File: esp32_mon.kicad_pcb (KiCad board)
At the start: 2 copper layers, 38.7 x 49.5 mm, 31 parts, among them J1 I2C, J2 UART, J3 BAT, J4 USB, Q1 NTJD1155L, Q2 MMDT3904, U1 ESP32, U2 TC4054GR, U3 RT9080-33GJ5S, U4 SHT40

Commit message: cleanup old project
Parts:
- U4: value SHT40 -> SHT4x; footprint SHT40:SHT40-AD1B-R2 -> parts:SHT4x
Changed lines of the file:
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@@
     (fp_line (start 0.88 1.45) (end -0.88 1.45) (layer "F.Fab") (width 0.1))
     (pad "1" smd rect locked (at -1.71 -0.95 90) (size 2 0.65) (layers "F.Cu" "F.Paste" "F.Mask")
-      (net 22 "Net-(R1-Pad2)") (pinfunction "CHRG") (pintype "unspecified"))
+      (net 22 "Net-(R1-Pad2)") (pinfunction "CHRG") (pintype "output"))
     (pad "2" smd rect locked (at -1.71 0 90) (size 2 0.65) (layers "F.Cu" "F.Paste" "F.Mask")
       (net 1 "GND") (pinfunction "GND") (pintype "power_in"))
     (pad "3" smd rect locked (at -1.71 0.95 90) (size 2 0.65) (layers "F.Cu" "F.Paste" "F.Mask")
-      (net 4 "+BATT") (pinfunction "BAT") (pintype "unspecified"))
+      (net 4 "+BATT") (pinfunction "BAT") (pintype "power_out"))
     (pad "4" smd rect locked (at 1.71 0.95 90) (size 2 0.65) (layers "F.Cu" "F.Paste" "F.Mask")
       (net 3 "VCC") (pinfunction "VCC") (pintype "power_in"))
     (pad "5" smd rect locked (at 1.71 -0.95 90) (size 2 0.65) (layers "F.Cu" "F.Paste" "F.Mask")
-      (net 23 "Net-(R2-Pad1)") (pinfunction "PROG") (pintype "unspecified"))
+      (net 23 "Net-(R2-Pad1)") (pinfunction "PROG") (pintype "input"))
     (model "${KICAD6_3DMODEL_DIR}/Package_TO_SOT_SMD.3dshapes/TSOT-23-5.wrl"
       (offset (xyz 0 0 0))
@@
       (net 24 "unconnected-(U3-Pad4)") (pinfunction "NC") (pintype "no_connect"))
     (pad "5" smd rect locked (at 1.71 -0.95 90) (size 2 0.65) (layers "F.Cu" "F.Paste" "F.Mask")
-      (net 2 "+3V3") (pinfunction "VOUT") (pintype "output"))
+      (net 2 "+3V3") (pinfunction "VOUT") (pintype "power_out"))
     (model "${KISYS3DMOD}/Package_TO_SOT_SMD.3dshapes/TSOT-23-5.wrl"
       (offset (xyz 0 0 0))
@@
     )
   )
-  (footprint "SHT40:SHT40-AD1B-R2" (layer "F.Cu")
+  (footprint "parts:SHT4x" (layer "F.Cu")
     (at 183.007 57.658 180)
     (property "Sheetfile" "esp32_mon.kicad_sch")
     (property "Sheetname" "")
     (attr through_hole)
-    (fp_text reference "U4" (at 0 2.54) (layer "F.SilkS") hide
-      (effects (font (size 1 1) (thickness 0.15)))
-    )
-    (fp_text value "SHT40" (at 2.54 0 270) (layer "F.SilkS")
-      (effects (font (size 1 1) (thickness 0.15)))
-    )
-    (fp_text user "*" (at 0 0) (layer "F.SilkS")
-      (effects (font (size 1 1) (thickness 0.15)))
-    )
-    (fp_text user "Copyright 2021 Accelerated Designs. All rights reserved." (at 0 0) (layer "Cmts.User")
+    (fp_text reference "U4" (at 0 2.54 180) (layer "F.SilkS")
+      (effects (font (size 1 1) (thickness 0.15)))
+    )
+    (fp_text value "SHT4x" (at 0 -2.54 180) (layer "F.SilkS")
+      (effects (font (size 1 1) (thickness 0.15)))
+    )
+    (fp_text user "*" (at 0 0 180) (layer "F.SilkS")
+      (effects (font (size 1 1) (thickness 0.15)))
+    )
+    (fp_text user "Copyright 2021 Accelerated Designs. All rights reserved." (at 0 0 180) (layer "Cmts.User")
       (effects (font (size 0.127 0.127) (thickness 0.002)))
     )
-    (fp_text user "*" (at 0 0) (layer "F.Fab")
-      (effects (font (size 1 1) (thickness 0.15)))
-    )
+    (fp_text user "*" (at 0 0 180) (layer "F.Fab")
+      (effects (font (size 1 1) (thickness 0.15)))
+    )
+    (fp_line (start -0.9271 0.9271) (end 0.9271 0.9271) (layer "F.SilkS") (width 0.12))
     (fp_line (start 0.9271 -0.9271) (end -0.9271 -0.9271) (layer "F.SilkS") (width 0.12))
-    (fp_line (start -0.9271 0.9271) (end 0.9271 0.9271) (layer "F.SilkS") (width 0.12))
     (fp_circle (center -1.950899 -0.4) (end -1.849299 -0.4) (layer "F.SilkS") (width 0.12) (fill none))
-    (fp_line (start -1.0541 1.0541) (end -1.0541 0.8068) (layer "F.CrtYd") (width 0.05))
-    (fp_line (start 1.0541 0.8068) (end 1.0541 1.0541) (layer "F.CrtYd") (width 0.05))
-    (fp_line (start 1.0541 -1.0541) (end 1.0541 -0.8068) (layer "F.CrtYd") (width 0.05))
+    (fp_line (start -1.0541 -0.8068) (end -1.0541 -1.0541) (layer "F.CrtYd") (width 0.05))
     (fp_line (start -1.0541 -1.0541) (end 1.0541 -1.0541) (layer "F.CrtYd") (width 0.05))
-    (fp_line (start 1.354099 -0.8068) (end 1.354099 0.8068) (layer "F.CrtYd") (width 0.05))
-    (fp_line (start -1.0541 -0.8068) (end -1.0541 -1.0541) (layer "F.CrtYd") (width 0.05))
-    (fp_line (start 1.354099 0.8068) (end 1.0541 0.8068) (layer "F.CrtYd") (width 0.05))
-    (fp_line (start -1.354099 -0.8068) (end -1.0541 -0.8068) (layer "F.CrtYd") (width 0.05))
-    (fp_line (start -1.0541 0.8068) (end -1.354099 0.8068) (layer "F.CrtYd") (width 0.05))
     (fp_line (start -1.354099 0.8068) (end -1.354099 -0.8068) (layer "F.CrtYd") (width 0.05))
     (fp_line (start 1.0541 1.0541) (end -1.0541 1.0541) (layer "F.CrtYd") (width 0.05))
+    (fp_line (start -1.354099 -0.8068) (end -1.0541 -0.8068) (layer "F.CrtYd") (width 0.05))
+    (fp_line (start 1.354099 -0.8068) (end 1.354099 0.8068) (layer "F.CrtYd") (width 0.05))
     (fp_line (start 1.0541 -0.8068) (end 1.354099 -0.8068) (layer "F.CrtYd") (width 0.05))
+    (fp_line (start 1.0541 -1.0541) (end 1.0541 -0.8068) (layer "F.CrtYd") (width 0.05))
+    (fp_line (start 1.354099 0.8068) (end 1.0541 0.8068) (layer "F.CrtYd") (width 0.05))
+    (fp_line (start -1.0541 1.0541) (end -1.0541 0.8068) (layer "F.CrtYd") (width 0.05))
+    (fp_line (start -1.0541 0.8068) (end -1.354099 0.8068) (layer "F.CrtYd") (width 0.05))
+    (fp_line (start 1.0541 0.8068) (end 1.0541 1.0541) (layer "F.CrtYd") (width 0.05))
     (fp_circle (center -1.601699 -0.4) (end -1.525499 -0.4) (layer "F.CrtYd") (width 0.05) (fill none))
+    (fp_line (start -0.8001 -0.8001) (end -0.8001 0.8001) (layer "F.Fab") (width 0.1))
     (fp_line (start -0.8001 0.8001) (end 0.8001 0.8001) (layer "F.Fab") (width 0.1))
-    (fp_line (start -0.8001 -0.8001) (end -0.8001 0.8001) (layer "F.Fab") (width 0.1))
     (fp_line (start 0.8001 -0.8001) (end -0.8001 -0.8001) (layer "F.Fab") (width 0.1))
     (fp_line (start 0.8001 0.8001) (end 0.8001 -0.8001) (layer "F.Fab") (width 0.1))

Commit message: minor cleanup
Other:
- board text added: "ESPmon 2.0"
- board text removed: "ESPmon rev2.0"
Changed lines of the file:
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@@
       (effects (font (size 1 1) (thickness 0.15)))
     )
-    (fp_text value "SHT4x" (at 0 -2.54 180) (layer "F.SilkS")
+    (fp_text value "SHT4x" (at 2.667 0 270) (layer "F.SilkS")
       (effects (font (size 1 1) (thickness 0.15)))
     )
@@
     (effects (font (size 1 1) (thickness 0.15)) (justify mirror))
   )
-  (gr_text "ESPmon\nrev2.0" (at 154.94 48.514) (layer "F.SilkS")
+  (gr_text "ESPmon\n2.0" (at 154.94 48.514) (layer "F.SilkS")
     (effects (font (size 1.5 1.5) (thickness 0.3)))
   )
@@
   (via (at 164.465 54.61) (size 0.8) (drill 0.4) (layers "F.Cu" "B.Cu") (free) (net 1))
   (via (at 172.72 64.77) (size 0.8) (drill 0.4) (layers "F.Cu" "B.Cu") (free) (net 1))
-  (via (at 163.195 90.17) (size 0.8) (drill 0.4) (layers "F.Cu" "B.Cu") (free) (net 1))
+  (via (at 151.511 68.453) (size 0.8) (drill 0.4) (layers "F.Cu" "B.Cu") (free) (net 1))
   (via (at 186.69 52.959) (size 0.8) (drill 0.4) (layers "F.Cu" "B.Cu") (free) (net 1))
   (via (at 186.69 88.265) (size 0.8) (drill 0.4) (layers "F.Cu" "B.Cu") (free) (net 1))
@@
   (via (at 180.975 58.42) (size 0.8) (drill 0.4) (layers "F.Cu" "B.Cu") (free) (net 1))
   (via (at 172.72 54.61) (size 0.8) (drill 0.4) (layers "F.Cu" "B.Cu") (free) (net 1))
-  (via (at 153.67 90.805) (size 0.8) (drill 0.4) (layers "F.Cu" "B.Cu") (free) (net 1))
+  (via (at 153.797 90.297) (size 0.8) (drill 0.4) (layers "F.Cu" "B.Cu") (free) (net 1))
   (segment (start 156.9935 54.1235) (end 156.845 53.975) (width 0.5) (layer "F.Cu") (net 2))
   (segment (start 175.641 72.898) (end 178.943 72.898) (width 0.25) (layer "F.Cu") (net 2))
@@
   (segment (start 152.908 83.312) (end 154.178 82.042) (width 0.25) (layer "F.Cu") (net 8))
   (segment (start 153.42501 75.82499) (end 154.94 74.31) (width 0.25) (layer "F.Cu") (net 8))
-  (segment (start 152.4 78.74) (end 152.4 78.724) (width 0.25) (layer "F.Cu") (net 8))
   (segment (start 153.42501 77.69899) (end 153.42501 75.82499) (width 0.25) (layer "F.Cu") (net 8))
   (segment (start 154.94 80.01) (end 154.686 79.756) (width 0.25) (layer "F.Cu") (net 8))

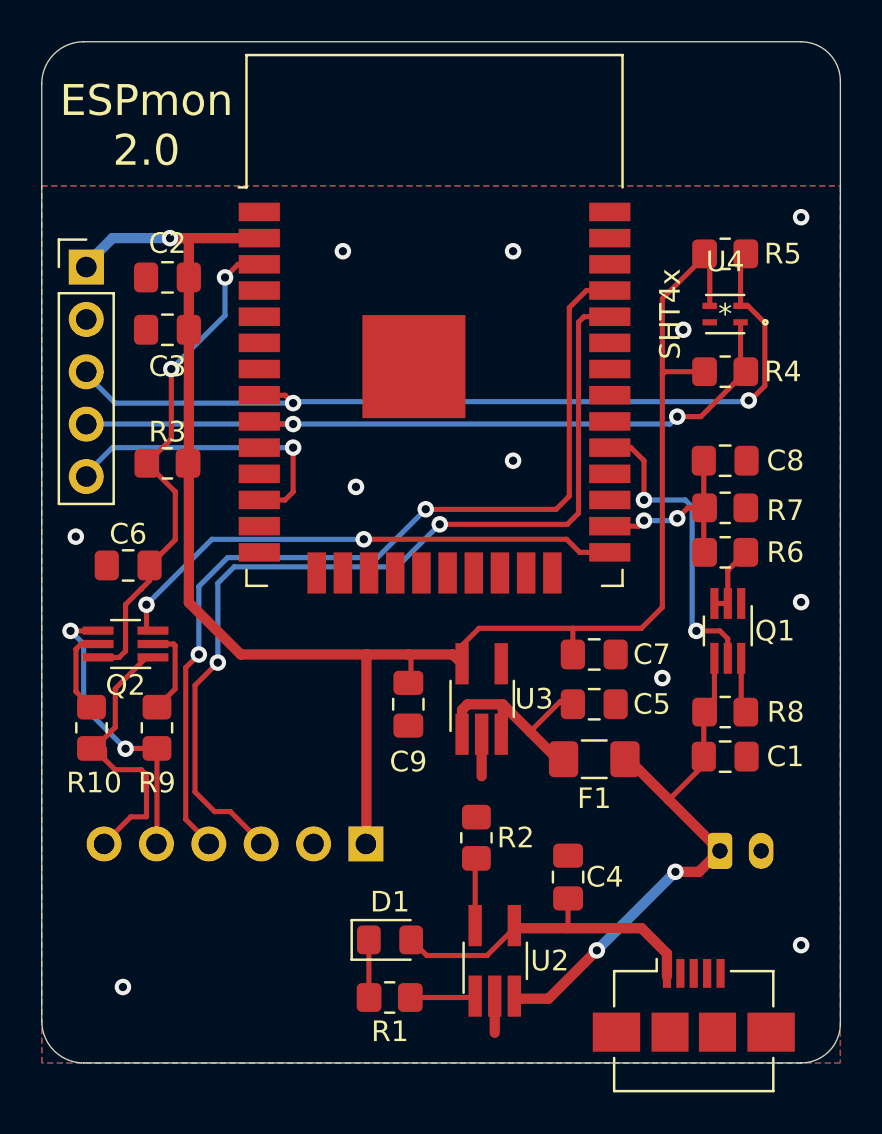
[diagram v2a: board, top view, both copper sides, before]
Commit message: update to availabe parts and tweaks
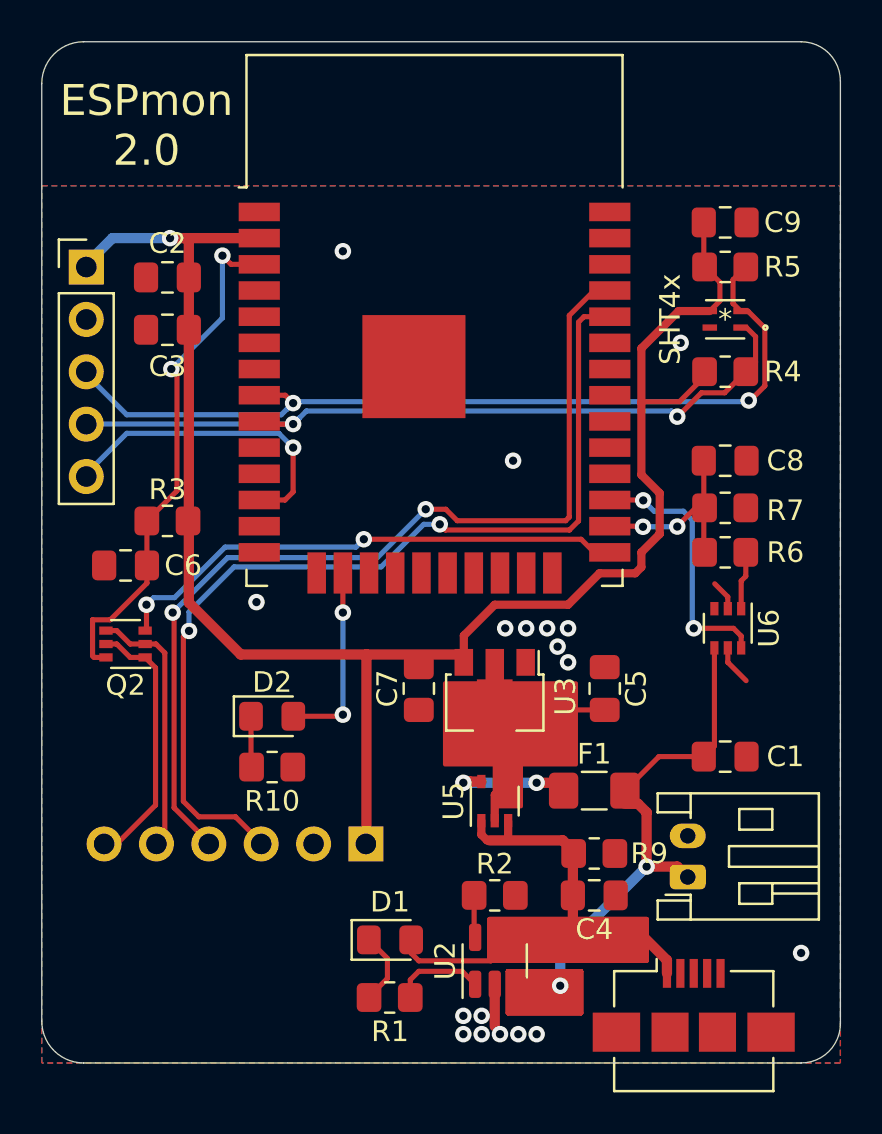
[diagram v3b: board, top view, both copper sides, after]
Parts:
- removed Q1: NTJD1155L, Package_TO_SOT_SMD:SOT-363_SC-70-6_Handsoldering
- removed R8: 1m, Resistor_SMD:R_0805_2012Metric_Pad1.20x1.40mm_HandSolder
- added D2: red, Diode_SMD:D_0805_2012Metric_Pad1.15x1.40mm_HandSolder, F.Cu at (161.0, 77.2)
- added U5: US5U30TR, Package_TO_SOT_SMD:SOT-353_SC-70-5, F.Cu at (171.8, 81.3)
- added U6: MIC9409x, Package_TO_SOT_SMD:SOT-363_SC-70-6, F.Cu at (183.1, 72.9)
- C1, C4: value 1u -> 4.7u
- J3: moved to F.Cu
- Q2: value MMDT3904 -> UMH3N; footprint Package_TO_SOT_SMD:SOT-363_SC-70-6_Handsoldering -> Package_TO_SOT_SMD:SOT-363_SC-70-6
- R10: value 10k -> 1k
- R9: value 10k -> 470k
- U2: value TC4054GR -> MCP73831-2-OT; footprint Package_TO_SOT_SMD:TSOT-23-5_HandSoldering -> Package_TO_SOT_SMD:SOT-23-5
- U3: value RT9080-33GJ5S -> MCP1700-3302E_SOT89; footprint Package_TO_SOT_SMD:TSOT-23-5_HandSoldering -> Package_TO_SOT_SMD:SOT-89-3
- moved C9 28.0 mm to (183.0, 53.2), turned to 0 degrees
- moved R9 22.1 mm to (176.7, 83.8), turned to 0 degrees
- moved R10 8.97 mm to (161.0, 79.6), turned to 0 degrees
- moved C7 8.67 mm to (168.1, 75.8), turned to -90 degrees
- moved R2 2.93 mm to (171.8, 85.9), turned to 0 degrees
- moved R3 2.79 mm to (156.0, 67.7)
- moved J3 2.01 mm to (181.2, 85.0), turned to 90 degrees
- moved C4 1.55 mm to (176.7, 85.9), turned to 0 degrees
- moved F1 1.52 mm to (176.7, 80.8)
- moved C5 0.92 mm to (177.2, 75.8), turned to 90 degrees
- moved U3 0.65 mm to (171.8, 76.2), turned to -90 degrees
- moved R5 0.63 mm to (183.0, 55.4)
- moved U4 0.25 mm to (183.0, 57.9)
- moved C6 0.13 mm to (153.9, 69.8)
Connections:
- F1 pad 2: Net-(C5-Pad1) -> Net-(F1-Pad2)
- Q2 pad 2: Net-(Q2-Pad2) -> /DTR
- Q2 pad 5: Net-(Q2-Pad5) -> /RTS
- R10 pad 1: Net-(Q2-Pad5) -> Net-(D2-Pad1)
- R10 pad 2: /RTS -> GND
- R9 pad 1: Net-(Q2-Pad2) -> VCC
- R9 pad 2: /DTR -> GND
- U1 pad 16: unconnected-(U1-Pad16) -> /LED
- U1 pad 27: unconnected-(U1-Pad27) -> /ADC_E
- U1 pad 29: /ADC_E -> unconnected-(U1-Pad29)
- U3 pad 1: Net-(C5-Pad1) -> GND
- U3 pad 2: GND -> Net-(C5-Pad1)
- U3 pad 3: Net-(C5-Pad1) -> +3V3
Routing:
- net VCC: track 16.4 -> 64.6 mm
- net +BATT: track 26.5 -> 60.2 mm
- net Net-(C5-Pad1): track 11.1 -> 22.2 mm
- net /LED: track 0.00 -> 9.31 mm, vias 0 -> 2
- net Net-(F1-Pad2): track 0.00 -> 5.92 mm, vias 0 -> 2
- net Net-(Q2-Pad5): track 5.19 -> 0.00 mm
- net Net-(Q2-Pad2): track 4.46 -> 0.00 mm
- net /DTR: track 14.7 -> 12.2 mm, vias 2 -> 0
- net Net-(D2-Pad1): track 0.00 -> 2.39 mm
- net Net-(Q1-Pad6): track 2.38 -> 0.00 mm
- net /ADC_E: track 15.0 -> 12.7 mm
- net GND: track 3.69 -> 5.47 mm, vias 11 -> 18
- net /RXD: track 44.6 -> 46.2 mm
- net /RTS: track 13.6 -> 12.2 mm
- net +3V3: track 86.6 -> 85.4 mm
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- added copper zone on F.Cu, net +BATT
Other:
- board text removed: "Li-Po 1S - +"

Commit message: esp32_mon.kicad_pcb: minor cleanup
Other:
- board text added: "+ -"
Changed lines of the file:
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@@
     (property "Sheetname" "")
     (attr smd)
-    (fp_text reference "R9" (at 2.667 0) (layer "F.SilkS")
+    (fp_text reference "R9" (at -2.794 0) (layer "F.SilkS")
       (effects (font (size 1 1) (thickness 0.15)))
     )
@@
     (effects (font (size 1 1) (thickness 0.15)) (justify mirror))
   )
+  (gr_text "+ -" (at 179.451 83.947 90) (layer "F.SilkS")
+    (effects (font (size 1 1) (thickness 0.15)))
+  )
   (gr_text "ESPmon\n2.0" (at 154.94 48.514) (layer "F.SilkS")
